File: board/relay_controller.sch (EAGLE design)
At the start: 69 parts, among them IC1 STM32F103C8T, IC3 AT24C, X1 RJ45-8L21-S, X2 RJ45-8L21-S

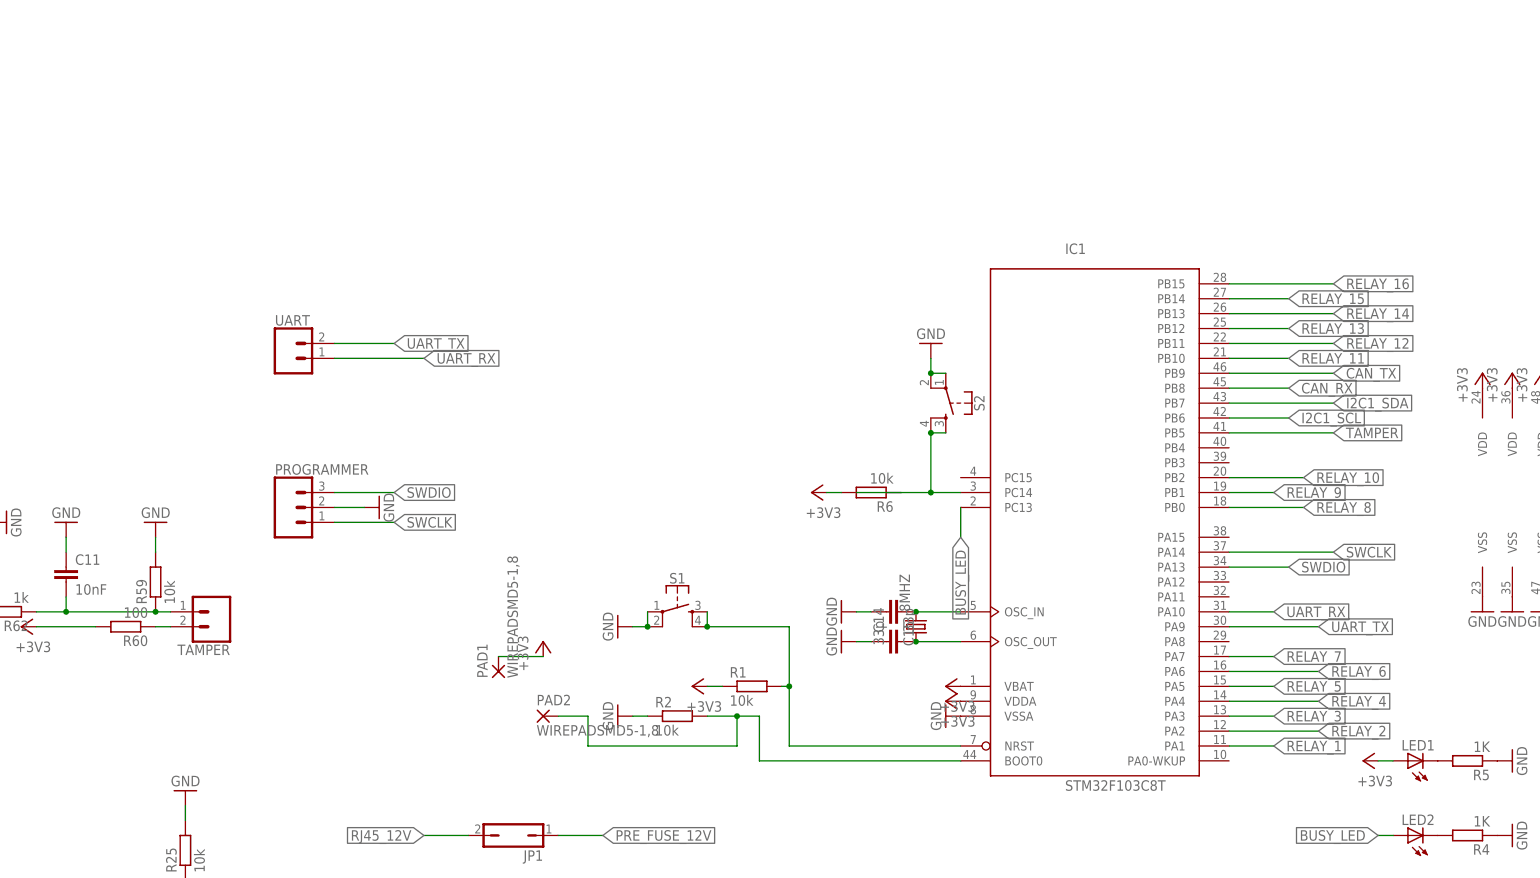
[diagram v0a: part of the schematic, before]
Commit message: jumpers for boot mode
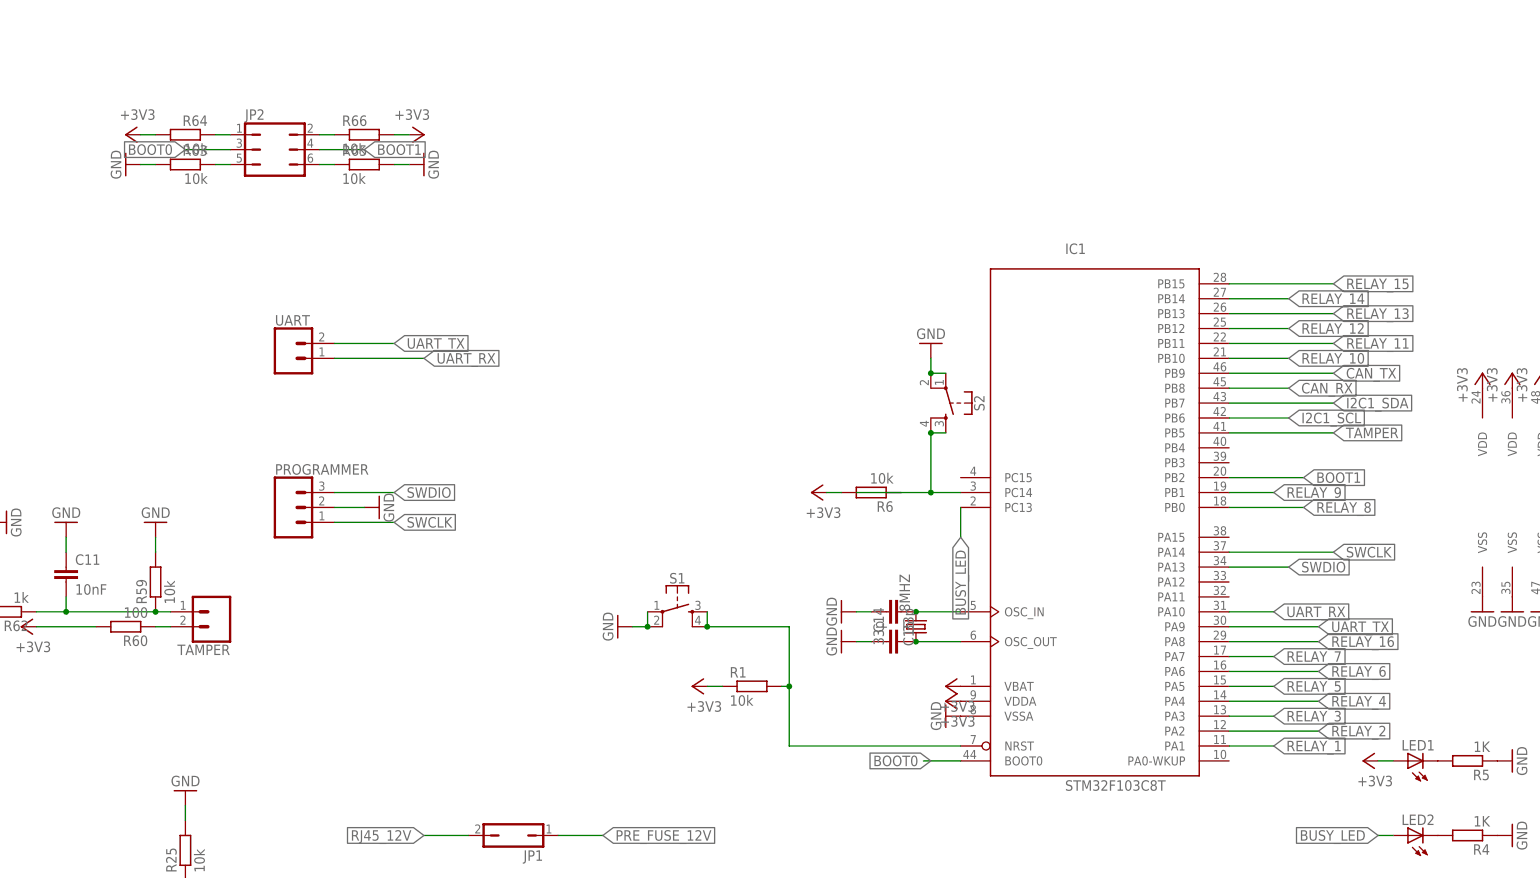
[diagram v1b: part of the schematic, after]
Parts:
- removed PAD1, PAD2: WIREPADSMD5-1,8, wirepad:WIREPADSMD5-1,8
- removed R2: 10k, rcl:R-EU_R0603
- added JP2: (no value), jumper:JP3Q
- added R63, R64, R65, R66: 10k, rcl:R-EU_R0603
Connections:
- removed net N$12: IC1MCU.BOOT0, PAD2.P, R2.2
- new net BOOT0: IC1MCU.BOOT0, JP2.3
- new net BOOT1: IC1MCU.PB2, JP2.4
- new net N$29: JP2.2, R66.1
- new net N$30: JP2.1, R64.1
- new net N$31: JP2.6, R65.1
- new net N$32: JP2.5, R63.1
- net +3V3: now also R64.2, R66.2; no longer PAD1.P
- net GND: now also R63.2, R65.2; no longer R2.1
- net RELAY_10: now also IC1MCU.PB10; no longer IC1MCU.PB2
- net RELAY_11: now also IC1MCU.PB11; no longer IC1MCU.PB10
- net RELAY_12: now also IC1MCU.PB12; no longer IC1MCU.PB11
- net RELAY_13: now also IC1MCU.PB13; no longer IC1MCU.PB12
- net RELAY_14: now also IC1MCU.PB14; no longer IC1MCU.PB13
- net RELAY_15: now also IC1MCU.PB15; no longer IC1MCU.PB14
- net RELAY_16: now also IC1MCU.PA8; no longer IC1MCU.PB15

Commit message: change to solderable boot jumper
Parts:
- removed JP2: (no value), jumper:JP3Q
- added SJ1, SJ2: (no value), jumper:SJ2W
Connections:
- net BOOT0: now also SJ1.2; no longer JP2.3
- net BOOT1: now also SJ2.2; no longer JP2.4
- net N$29: now also SJ2.1; no longer JP2.2
- net N$30: now also SJ1.1; no longer JP2.1
- net N$31: now also SJ2.3; no longer JP2.6
- net N$32: now also SJ1.3; no longer JP2.5
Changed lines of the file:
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@@
 <part name="+3V33" library="supply1" deviceset="+3V3" device=""/>
 <part name="+3V34" library="supply1" deviceset="+3V3" device=""/>
-<part name="JP2" library="jumper" deviceset="JP3Q" device=""/>
+<part name="SJ1" library="jumper" deviceset="SJ2W" device=""/>
+<part name="SJ2" library="jumper" deviceset="SJ2W" device=""/>
 </parts>
 <sheets>
@@
 <instance part="+3V33" gate="G$1" x="-187.96" y="147.32" rot="MR270"/>
 <instance part="+3V34" gate="G$1" x="-137.16" y="147.32" rot="R270"/>
-<instance part="JP2" gate="B" x="-162.56" y="144.78" rot="R270"/>
+<instance part="SJ1" gate="G$1" x="-165.1" y="144.78"/>
+<instance part="SJ2" gate="G$1" x="-160.02" y="144.78" rot="MR0"/>
 </instances>
 <busses>
@@
 <wire x1="-154.94" y1="144.78" x2="-147.32" y2="144.78" width="0.1524" layer="91"/>
 <label x="-147.32" y="144.78" size="1.778" layer="95" xref="yes"/>
-<pinref part="JP2" gate="B" pin="4"/>
+<pinref part="SJ2" gate="G$1" pin="2"/>
 </segment>
 <segment>
@@
 <wire x1="-170.18" y1="144.78" x2="-177.8" y2="144.78" width="0.1524" layer="91"/>
 <label x="-177.8" y="144.78" size="1.778" layer="95" rot="MR0" xref="yes"/>
-<pinref part="JP2" gate="B" pin="3"/>
+<pinref part="SJ1" gate="G$1" pin="2"/>
 </segment>
 <segment>
@@
 <wire x1="-154.94" y1="147.32" x2="-152.4" y2="147.32" width="0.1524" layer="91"/>
 <pinref part="R66" gate="G$1" pin="1"/>
-<pinref part="JP2" gate="B" pin="2"/>
+<pinref part="SJ2" gate="G$1" pin="1"/>
+<wire x1="-160.02" y1="149.86" x2="-154.94" y2="149.86" width="0.1524" layer="91"/>
+<wire x1="-154.94" y1="149.86" x2="-154.94" y2="147.32" width="0.1524" layer="91"/>
 </segment>
 </net>
@@
 <wire x1="-170.18" y1="147.32" x2="-172.72" y2="147.32" width="0.1524" layer="91"/>
 <pinref part="R64" gate="G$1" pin="1"/>
-<pinref part="JP2" gate="B" pin="1"/>
+<pinref part="SJ1" gate="G$1" pin="1"/>
+<wire x1="-165.1" y1="149.86" x2="-170.18" y2="149.86" width="0.1524" layer="91"/>
+<wire x1="-170.18" y1="149.86" x2="-170.18" y2="147.32" width="0.1524" layer="91"/>
 </segment>
 </net>
@@
 <wire x1="-154.94" y1="142.24" x2="-152.4" y2="142.24" width="0.1524" layer="91"/>
 <pinref part="R65" gate="G$1" pin="1"/>
-<pinref part="JP2" gate="B" pin="6"/>
+<pinref part="SJ2" gate="G$1" pin="3"/>
+<wire x1="-160.02" y1="139.7" x2="-154.94" y2="139.7" width="0.1524" layer="91"/>
+<wire x1="-154.94" y1="139.7" x2="-154.94" y2="142.24" width="0.1524" layer="91"/>
 </segment>
 </net>
@@
 <wire x1="-170.18" y1="142.24" x2="-172.72" y2="142.24" width="0.1524" layer="91"/>
 <pinref part="R63" gate="G$1" pin="1"/>
-<pinref part="JP2" gate="B" pin="5"/>
-</segment>
-</net>
+<pinref part="SJ1" gate="G$1" pin="3"/>
+<wire x1="-165.1" y1="139.7" x2="-170.18" y2="139.7" width="0.1524" layer="91"/>
+<wire x1="-170.18" y1="139.7" x2="-170.18" y2="142.24" width="0.1524" layer="91"/>
+</segment>
+</net>

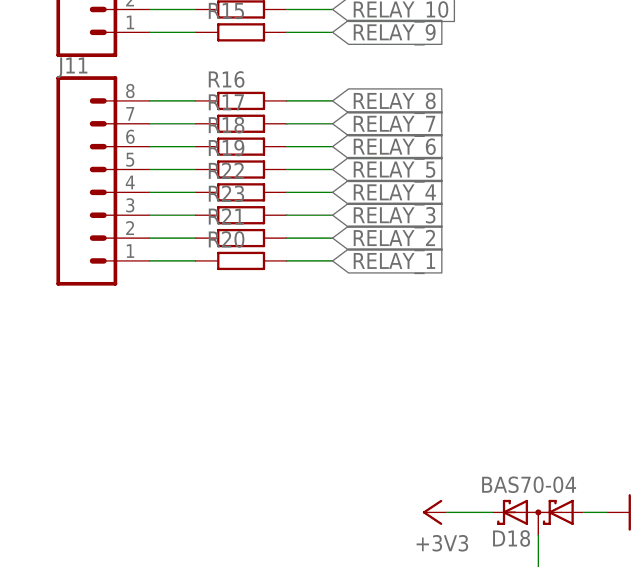
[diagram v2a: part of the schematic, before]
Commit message: value for current limiting resistor
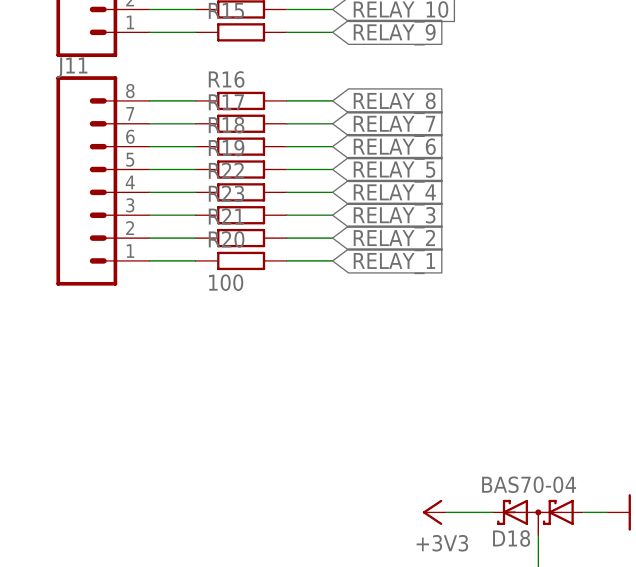
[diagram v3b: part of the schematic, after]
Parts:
- R20: value (none) -> 100
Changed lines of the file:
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@@
 <part name="R18" library="resistor" deviceset="R-EU_" device="R0603"/>
 <part name="R19" library="resistor" deviceset="R-EU_" device="R0603"/>
-<part name="R20" library="resistor" deviceset="R-EU_" device="R0603"/>
+<part name="R20" library="resistor" deviceset="R-EU_" device="R0603" value="100"/>
 <part name="R21" library="resistor" deviceset="R-EU_" device="R0603"/>
 <part name="R22" library="resistor" deviceset="R-EU_" device="R0603"/>

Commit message: change 16 driver pin to 5 relay output (g6k-2f-y)
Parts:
- removed J11: (no value), SparkFun-Connectors:CONN_083.5MM-8
- removed JP1: (no value), jumper:JP1Q
- removed R12, R13, R14, R15, R16, R17, R18, R19, R21, R22, R23: (no value), resistor:R-EU_R0603
- removed R20: 100, resistor:R-EU_R0603
- removed TAMPER: (no value), SparkFun-Connectors:CONN_023.5MM
- removed X1, X2: RJ45-8L21-S, con-tycoelectronics:RJ45-8L21-S
- added D1, D2, D3, D4, D6: (no value), diode:DIODE-DO-214AC
- added J21, J5: (no value), SparkFun-Connectors:CONN_03SCREW
- added JP2: (no value), jumper:JP1Q
- added K1, K2, K3, K7, K8: G6K-2F-Y, relay:G6K-2F-Y
- added Q1, Q2, Q3, Q4, Q5: 220mA/50V/3.5Ω, SparkFun-DiscreteSemi:MOSFET-NCH-BSS138
- added R2: 10k, rcl:R-EU_R0603
- added X3, X4: (no value), con-molex-micro-fit-3_0:HEADER_POS8_43045-0812
- J1: device SparkFun-Connectors:CONN_03-SCREW-5MM -> SparkFun-Connectors:CONN_03SCREW
- J2: device SparkFun-Connectors:CONN_03SCREW -> SparkFun-Connectors:CONN_023.5MM
- J3: device SparkFun-Connectors:CONN_023.5MM -> SparkFun-Connectors:CONN_03SCREW
- R10, R11, R8, R9: value (none) -> 10k; device resistor:R-EU_R0603 -> rcl:R-EU_R0603
- R25: value 10k -> 120
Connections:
- removed net N$20: R25.1, X1.S@1, X1.S@2, X2.S@1, X2.S@2
- removed net RELAY_10: IC1MCU.PB10, R14.2
- removed net RELAY_11: IC1MCU.PB11, R13.2
- removed net RELAY_13: IC1MCU.PB13, R11.2
- removed net RELAY_14: IC1MCU.PB14, R10.2
- removed net RELAY_15: IC1MCU.PB15, R9.2
- removed net RJ45_12V: JP1.2, X1.4, X1.5, X1.6, X2.4, X2.5, X2.6
- new net N$12: JP2.2, R25.1
- new net N$33: J5.1, K32.O, K33.O
- new net N$34: J5.3, K32.S, K33.S
- new net N$35: J5.2, K32.P, K33.P
- new net N$36: D6.A, K31.-, Q5.D
- net +12V: now also D1.C, D2.C, D3.C, D4.C, D6.C, K11.+, K21.+, K31.+, K71.+, K81.+
- net +3V3: no longer J1.1
- net CAN_H: now also R25.2, X3.1, X4.1; no longer X1.1, X2.1
- net CAN_L: now also JP2.1, X3.5, X4.5; no longer X1.2, X2.2
- net GND: now also Q1.S, Q2.S, Q3.S, Q4.S, Q5.S, R10.2, R11.2, R2.2, R8.2, R9.2, X3.6, X3.7, X3.8, X4.6, X4.7, X4.8; no longer J1.3, R25.2, X1.3, X1.7, X1.8, X2.3, X2.7, X2.8
- net N$10: now also J2.2; no longer TAMPER.2
- net N$13: now also J21.3, K72.S, K73.S; no longer J2.3, R10.1
- net N$14: now also J21.2, K72.P, K73.P; no longer J2.2, R11.1
- net N$15: now also D1.A, K71.-, Q3.D; no longer J2.1, R12.1
- net N$16: now also J1.3, K82.S, K83.S; no longer J4.3, R13.1
- net N$18: now also J1.2, K82.P, K83.P; no longer J4.2, R14.1
- net N$19: now also D2.A, K81.-, Q1.D; no longer J4.1, R15.1
- net N$21: now also J3.1, K12.O, K13.O; no longer J11.8, R16.1
- net N$22: now also J3.3, K12.S, K13.S; no longer J11.7, R17.1
- net N$23: now also J3.2, K12.P, K13.P; no longer J11.6, R18.1
- net N$24: now also D3.A, K11.-, Q2.D; no longer J11.5, R19.1
- net N$25: now also J4.1, K22.O, K23.O; no longer J11.1, R20.1
- net N$26: now also J4.3, K22.S, K23.S; no longer J11.2, R21.1
- net N$27: now also J4.2, K22.P, K23.P; no longer J11.4, R22.1
- net N$28: now also D4.A, K21.-, Q4.D; no longer J11.3, R23.1
- net N$4: now also J21.1, K72.O, K73.O; no longer J3.2, R8.1
- net N$5: now also J2.1; no longer TAMPER.1
- net N$9: now also J1.1, K82.O, K83.O; no longer J3.1, R9.1
- net PRE_FUSE_12V: now also X3.2, X3.3, X3.4, X4.2, X4.3, X4.4; no longer J1.2, JP1.1
- net RELAY_1: now also Q1.G, R2.1; no longer R20.2
- net RELAY_12: no longer R12.2
- net RELAY_16: no longer R8.2
- net RELAY_2: now also Q3.G, R9.1; no longer R21.2
- net RELAY_3: now also Q2.G, R8.1; no longer R23.2
- net RELAY_4: now also Q4.G, R10.1; no longer R22.2
- net RELAY_5: now also Q5.G, R11.1; no longer R19.2
- net RELAY_6: no longer R18.2
- net RELAY_7: no longer R17.2
- net RELAY_8: no longer R16.2
- net RELAY_9: no longer R15.2

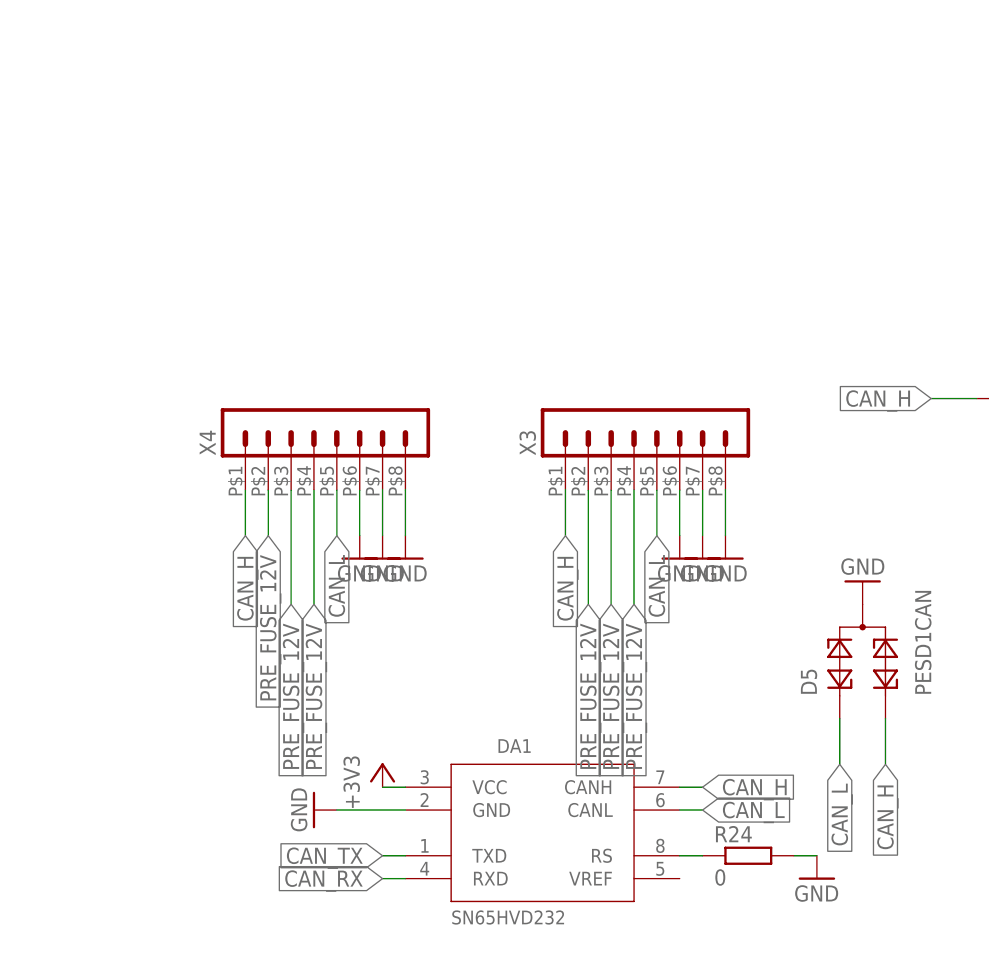
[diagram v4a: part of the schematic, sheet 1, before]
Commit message: more distance between rj45 connectors
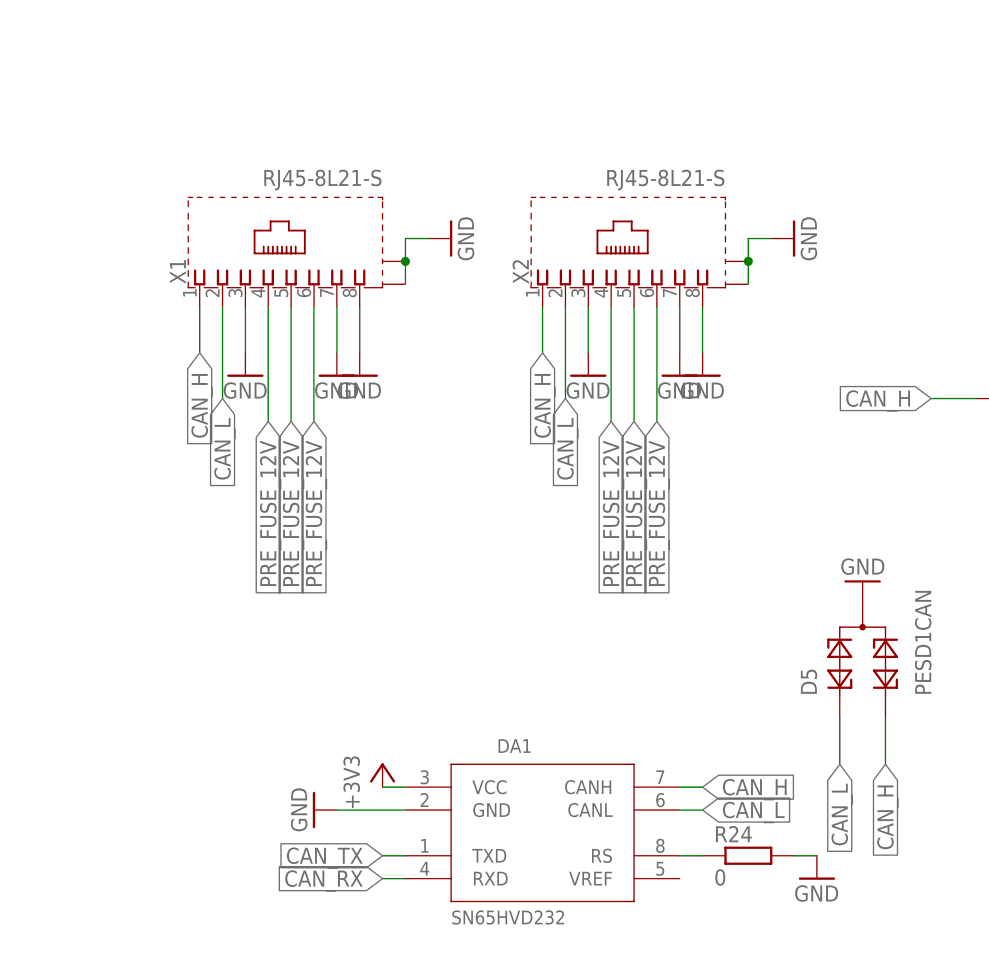
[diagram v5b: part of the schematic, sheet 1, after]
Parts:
- removed X3, X4: (no value), con-molex-micro-fit-3_0:HEADER_POS8_43045-0812
- added X1, X2: RJ45-8L21-S, con-tycoelectronics:RJ45-8L21-S
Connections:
- net CAN_H: now also X1.1, X2.1; no longer X3.1, X4.1
- net CAN_L: now also X1.2, X2.2; no longer X3.5, X4.5
- net GND: now also X1.3, X1.7, X1.8, X1.S@1, X1.S@2, X2.3, X2.7, X2.8, X2.S@1, X2.S@2; no longer X3.6, X3.7, X3.8, X4.6, X4.7, X4.8
- net PRE_FUSE_12V: now also X1.4, X1.5, X1.6, X2.4, X2.5, X2.6; no longer X3.2, X3.3, X3.4, X4.2, X4.3, X4.4

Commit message: change to packages with place drawing
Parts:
- removed C11: 10nF, eagle-ltspice:CC0603
- removed C14, C15: 33p, rcl:C-EUC0603
- removed C3, C8: 100n, rcl:C-EUC0603
- removed C7: 1u, rcl:C-EUC0603
- added C12, C13, C16, C17, C19, C20: 100n, microbuilder:CAP_CERAMIC0603
- added F4: 6V/0.5A, SparkFun-Fuses:PPTC_HALF-AMP
- C1, C5, C6: value 100n -> 1u; device rcl:C-EUC0603 -> microbuilder:CAP_CERAMIC0603
- C10: value 100n -> 33pf; device rcl:C-EUC0603 -> microbuilder:CAP_CERAMIC0603
- C2: value 1u -> 10nF; device rcl:C-EUC0603 -> microbuilder:CAP_CERAMIC0603
- C4: value 1u -> 33pf; device rcl:C-EUC0603 -> microbuilder:CAP_CERAMIC0603
- C9: device rcl:C-EUC0603 -> microbuilder:CAP_CERAMIC0603
- F2: value 12V/50mA -> 6V/0.5A
- R1, R10, R11, R2, R24, R25, R27, R3, R4, R5, R59, R6, R60, R61, R62, R63, R64, R65, R66, R8, R9: device rcl:R-EU_R0603 -> microbuilder:RESISTOR0603
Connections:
- net +3V3: now also C1.P$1, C12.P$1, C13.P$1, C16.P$1, C17.P$1, C19.P$1, C20.P$1, C5.P$1, C6.P$1, C9.P$1; no longer C1.1, C10.1, C2.1, C3.1, C4.1, C5.1, C6.1, C7.1, C8.1, C9.1
- net GND: now also C1.P$2, C10.P$1, C12.P$2, C13.P$2, C16.P$2, C17.P$2, C19.P$2, C2.P$1, C20.P$2, C4.P$1, C5.P$2, C6.P$2, C9.P$2; no longer C1.2, C10.2, C11.1, C14.1, C15.2, C2.2, C3.2, C4.2, C5.2, C6.2, C7.2, C8.2, C9.2
- net N$1: now also C4.P$2; no longer C15.1
- net N$2: now also C10.P$2; no longer C14.2
- net N$5: now also C2.P$2; no longer C11.2
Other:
- moved on the sheet: C1, C10, C2, C4, C5, C6, C9
